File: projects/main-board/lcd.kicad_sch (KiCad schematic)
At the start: 10 parts, among them J6 NHD-4.3-480272EF-ASXP (Molex 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

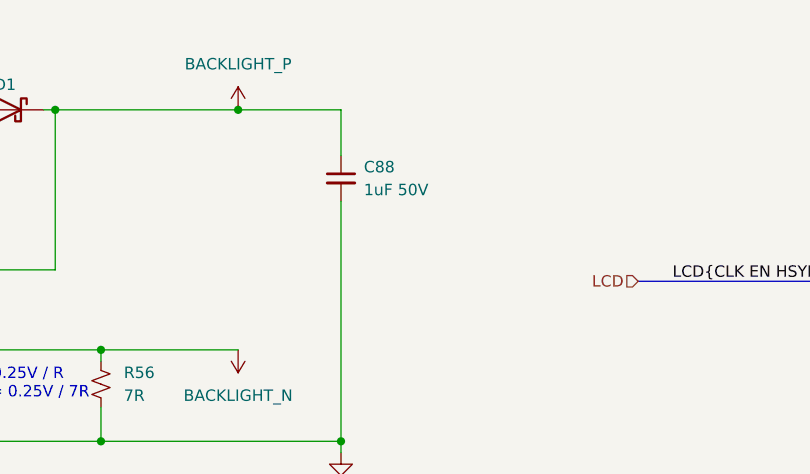
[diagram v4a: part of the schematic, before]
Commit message: Normalise capacitors
- Add capacitor parts to library.
- Replace all placeholder capacitors
  with the actual part numbers.
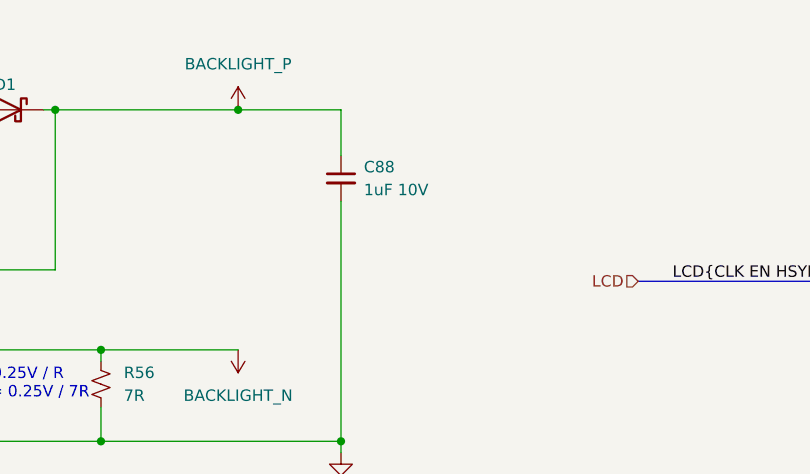
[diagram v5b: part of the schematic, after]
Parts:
- removed C87, C89: 1uF 10V, symbol Device:C_Small
- removed C88: 1uF 50V, symbol Device:C_Small
- removed C90: 100nF 10V, symbol Device:C_Small
- added C87, C88, C89: 1uF 10V, Capacitor_SMD:C_0402_1005Metric, symbol symbol-library-capacitors:CC0402KRX5R6BB105
- added C90: 100nF 10V, Capacitor_SMD:C_0402_1005Metric, symbol symbol-library-capacitors:CC0402KRX7R6BB104
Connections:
- net 3V3: now also C89.1, C90.1
- net BACKLIGHT_P: now also C88.1
- net GND: now also C87.2, C88.2, C89.2, C90.2
- net VSYS: now also C87.1

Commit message: Replace placeholder resistors
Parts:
- removed R55: 10K, symbol Device:R_Small_US
- removed R56: 7R, symbol Device:R_Small_US
- added R51: 10K, Resistor_SMD:R_0402_1005Metric, symbol symbol-library-resistors:RC0402JR-0710KL
- added R52: 6.81R, Resistor_SMD:R_0402_1005Metric, symbol symbol-library-resistors:RC0402FR-076R81L
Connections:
- net BACKLIGHT_N: now also R52.1
- net BACKLIGHT_PWM: now also R51.1
- net GND: now also R51.2, R52.2
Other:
- note added: "I = 0.25V / R 36mA = 0.25V / 6.81R"
- note removed: "I = 0.25V / R 35mA = 0.25V / 7R"
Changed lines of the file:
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@@
 	(generator_version "9.0")
 	(paper "A4")
-	(text "I = 0.25V / R\n35mA = 0.25V / 7R"
+	(text "I = 0.25V / R\n36mA = 0.25V / 6.81R"
 		(exclude_from_sim no)
 		(at 85.598 72.39 0)
@@
 	)
 	(symbol
-		(lib_id "Device:R_Small_US")
-		(at 95.25 72.39 0)
-		(unit 1)
-		(exclude_from_sim no)
-		(in_bom yes)
-		(on_board yes)
-		(dnp no)
-		(fields_autoplaced yes)
-		(property "Reference" "R56"
-			(at 97.79 71.1199 0)
-			(effects
-				(font
-					(size 1.27 1.27)
-				)
-				(justify left)
-			)
-		)
-		(property "Value" "7R"
-			(at 97.79 73.6599 0)
-			(effects
-				(font
-					(size 1.27 1.27)
-				)
-				(justify left)
-			)
-		)
-		(property "Footprint" ""
-			(at 95.25 72.39 0)
-			(effects
-				(font
-					(size 1.27 1.27)
-				)
-				(hide yes)
-			)
-		)
-		(property "Datasheet" "~"
-			(at 95.25 72.39 0)
-			(effects
-				(font
-					(size 1.27 1.27)
-				)
-				(hide yes)
-			)
-		)
-		(property "Description" "Resistor, small US symbol"
-			(at 95.25 72.39 0)
-			(effects
-				(font
-					(size 1.27 1.27)
-				)
-				(hide yes)
-			)
-		)
-		(pin "2"
-		)
-		(pin "1"
-		)
-		(instances
-			(project "main-board"
-				(path "/c621b5fd-2ef7-4a67-960d-0ffc72b1245a/295cf080-cb0b-4f37-9a57-f3f4472bf120"
-					(reference "R56")
-					(unit 1)
-				)
-			)
-		)
-	)
-	(symbol
 		(lib_id "symbol-library:AP5725WG-7")
 		(at 58.42 48.26 0)
@@
 	)
 	(symbol
+		(lib_id "symbol-library-resistors:RC0402JR-0710KL")
+		(at 44.45 82.55 0)
+		(unit 1)
+		(exclude_from_sim no)
+		(in_bom yes)
+		(on_board yes)
+		(dnp no)
+		(fields_autoplaced yes)
+		(property "Reference" "R51"
+			(at 46.99 81.2799 0)
+			(effects
+				(font
+					(size 1.27 1.27)
+				)
+				(justify left)
+			)
+		)
+		(property "Value" "10K"
+			(at 46.99 83.8199 0)
+			(effects
+				(font
+					(size 1.27 1.27)
+				)
+				(justify left)
+			)
+		)
+		(property "Footprint" "Resistor_SMD:R_0402_1005Metric"
+			(at 44.45 82.55 0)
+			(effects
+				(font
+					(size 1.27 1.27)
+				)
+				(hide yes)
+			)
+		)
+		(property "Datasheet" "~"
+			(at 44.45 82.55 0)
+			(effects
+				(font
+					(size 1.27 1.27)
+				)
+				(hide yes)
+			)
+		)
+		(property "Description" "Resistor, small US symbol"
+			(at 44.45 82.55 0)
+			(effects
+				(font
+					(size 1.27 1.27)
+				)
+				(hide yes)
+			)
+		)
+		(pin "1"
+		)
+		(pin "2"
+		)
+		(instances
+			(project "main-board"
+				(path "/c621b5fd-2ef7-4a67-960d-0ffc72b1245a/295cf080-cb0b-4f37-9a57-f3f4472bf120"
+					(reference "R51")
+					(unit 1)
+				)
+			)
+		)
+	)
+	(symbol
 		(lib_id "power:VCC")
 		(at 110.49 41.91 0)
@@
 	)
 	(symbol
-		(lib_id "Device:R_Small_US")
-		(at 44.45 82.55 0)
+		(lib_id "symbol-library-resistors:RC0402FR-076R81L")
+		(at 95.25 72.39 0)
 		(unit 1)
 		(exclude_from_sim no)
@@
 		(dnp no)
 		(fields_autoplaced yes)
-		(property "Reference" "R55"
-			(at 46.99 81.2799 0)
+		(property "Reference" "R52"
+			(at 97.79 71.1199 0)
 			(effects
 				(font
@@
 			)
 		)
-		(property "Value" "10K"
-			(at 46.99 83.8199 0)
+		(property "Value" "6.81R"
+			(at 97.79 73.6599 0)
 			(effects
 				(font
@@
 			)
 		)
-		(property "Footprint" ""
-			(at 44.45 82.55 0)
+		(property "Footprint" "Resistor_SMD:R_0402_1005Metric"
+			(at 95.25 72.39 0)
 			(effects
 				(font
@@
 		)
 		(property "Datasheet" "~"
-			(at 44.45 82.55 0)
+			(at 95.25 72.39 0)
 			(effects
 				(font
@@
 		)
 		(property "Description" "Resistor, small US symbol"
-			(at 44.45 82.55 0)
+			(at 95.25 72.39 0)
 			(effects
 				(font
@@
 		)
 		(instances
-			(project "main-board"
+			(project ""
 				(path "/c621b5fd-2ef7-4a67-960d-0ffc72b1245a/295cf080-cb0b-4f37-9a57-f3f4472bf120"
-					(reference "R55")
+					(reference "R52")
 					(unit 1)
 				)

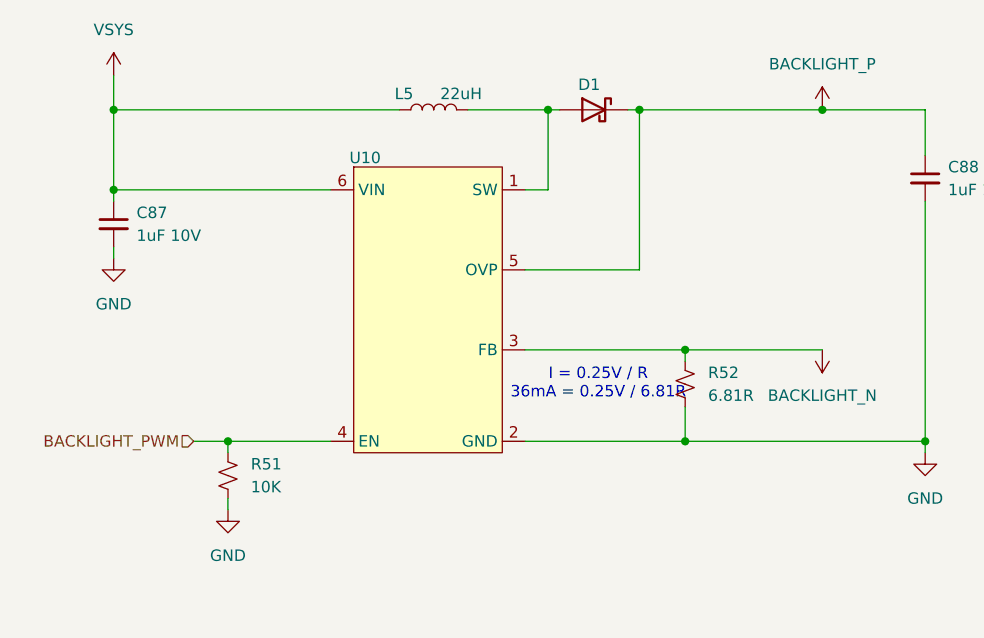
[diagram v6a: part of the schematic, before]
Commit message: Add footprints
- Inductors
- Switches
- Buttons
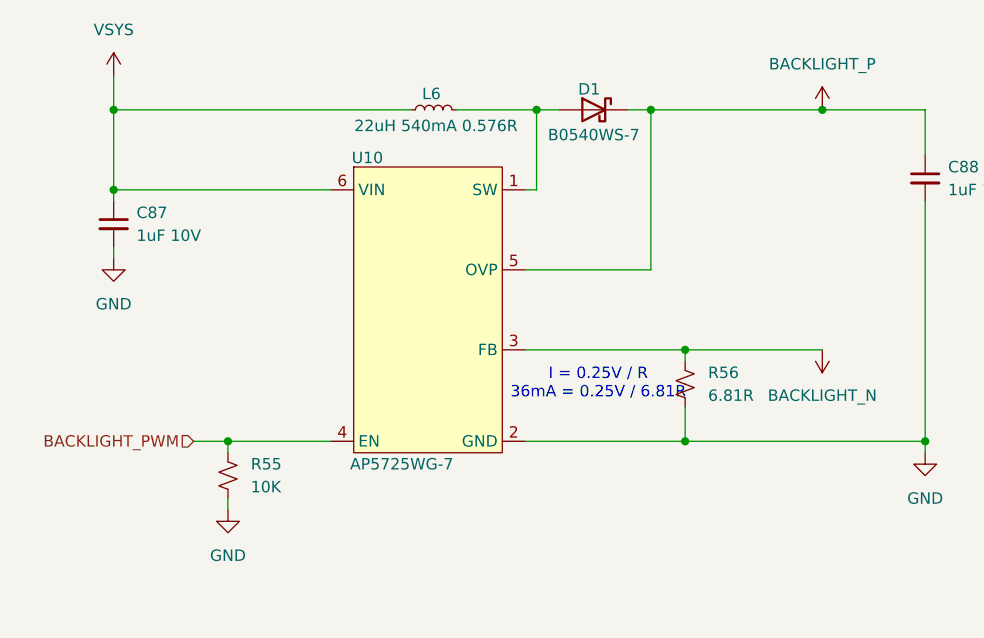
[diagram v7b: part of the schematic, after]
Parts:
- removed D1: D_Schottky, symbol Device:D_Schottky
- removed L5: 22uH, symbol Device:L
- added D1: B0540WS-7, footprint-library:SOD323_DIO, symbol symbol-library-diodes:B0540WS-7
- added L6: 22uH 540mA 0.576R, footprint-library:NR4012T220M, symbol symbol-library-inductors:NR4012T220M
- U10: value ~ -> AP5725WG-7; footprint (none) -> footprint-library:AP5725WG-7
- renumbered R51 to R55, R52 to R56
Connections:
- net BACKLIGHT_P: now also D1.1 (K)
- net VSYS: now also L6.1
- net at U10.1 (SW): now also D1.2 (A), L6.2

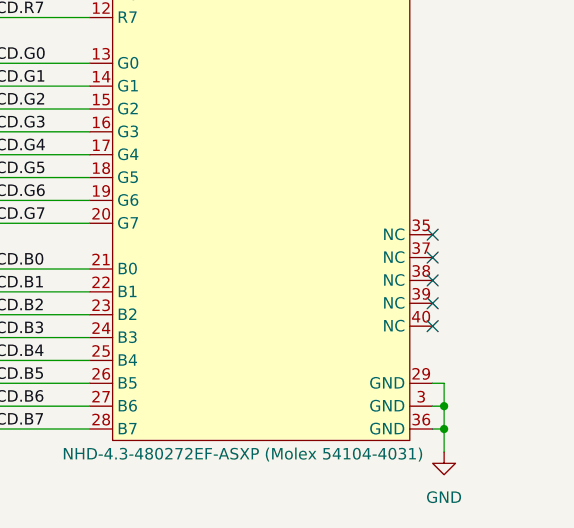
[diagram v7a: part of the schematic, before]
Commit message: Fix footprint DRC errors.
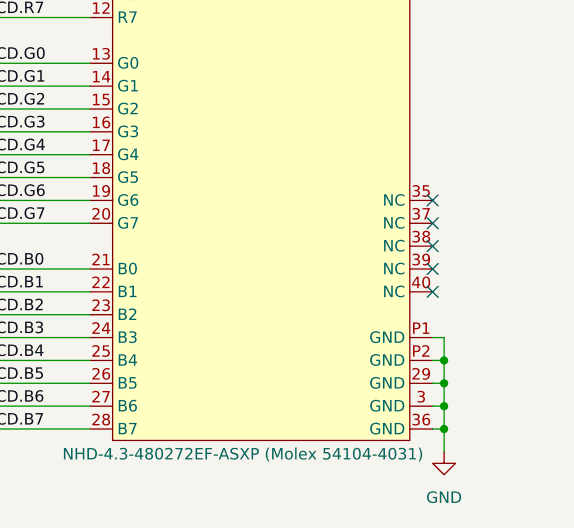
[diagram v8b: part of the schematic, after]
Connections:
- net GND: now also J6.P1 (GND), J6.P2 (GND)
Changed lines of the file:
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@@
+	)
+	(junction
+		(at 260.35 135.89)
+		(diameter 0)
+		(color 0 0 0 0)
 	)
 	(junction
@@
 	)
 	(junction
+		(at 260.35 138.43)
+		(diameter 0)
+		(color 0 0 0 0)
+	)
+	(junction
 		(at 260.35 143.51)
 		(diameter 0)
@@
 	)
 	(no_connect
-		(at 259.08 132.08)
+		(at 259.08 120.65)
 	)
 	(no_connect
-		(at 259.08 121.92)
+		(at 259.08 125.73)
 	)
 	(no_connect
-		(at 259.08 129.54)
+		(at 259.08 123.19)
 	)
 	(no_connect
-		(at 259.08 127)
+		(at 259.08 128.27)
 	)
 	(no_connect
-		(at 259.08 124.46)
+		(at 259.08 118.11)
 	)
 	(bus_entry
@@
 	(wire
 		(pts
+			(xy 259.08 133.35) (xy 260.35 133.35)
+		)
+		(stroke
+			(width 0)
+			(type default)
+		)
+	)
+	(wire
+		(pts
 			(xy 209.55 143.51) (xy 220.98 143.51)
 		)
@@
 		)
 	)
+	(wire
+		(pts
+			(xy 260.35 135.89) (xy 259.08 135.89)
+		)
+		(stroke
+			(width 0)
+			(type default)
+		)
+	)
 	(bus
 		(pts
@@
 		)
 	)
+	(wire
+		(pts
+			(xy 260.35 133.35) (xy 260.35 135.89)
+		)
+		(stroke
+			(width 0)
+			(type default)
+		)
+	)
 	(bus
 		(pts
@@
 		(pts
 			(xy 260.35 138.43) (xy 260.35 140.97)
+		)
+		(stroke
+			(width 0)
+			(type default)
+		)
+	)
+	(wire
+		(pts
+			(xy 260.35 138.43) (xy 260.35 135.89)
 		)
 		(stroke
@@
 	)
 	(symbol
-		(lib_name "NHD-4.3-480272EF-ASXP_1")
 		(lib_id "symbol-library:NHD-4.3-480272EF-ASXP")
 		(at 223.52 39.37 0)
@@
 		(pin "6"
 		)
+		(pin "P1"
+		)
+		(pin "P2"
+		)
 		(instances
